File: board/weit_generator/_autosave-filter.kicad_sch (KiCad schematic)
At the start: 5 parts, among them U1 MCP6004

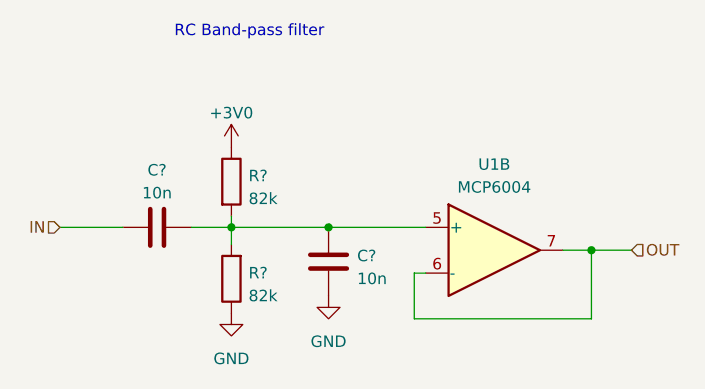
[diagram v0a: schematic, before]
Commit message: added filtering
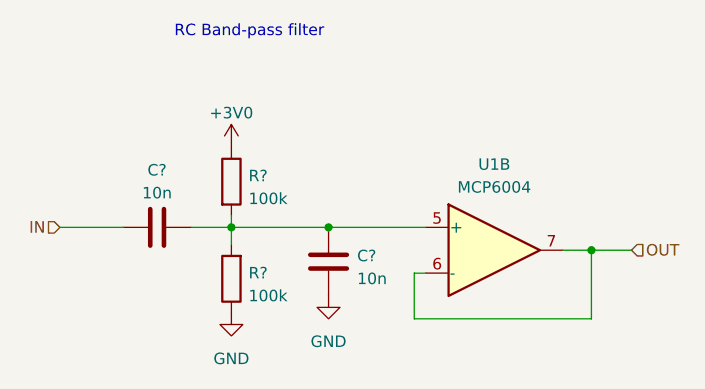
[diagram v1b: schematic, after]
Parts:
- R? (x2): value 82k -> 100k
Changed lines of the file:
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@@
       (effects (font (size 1.27 1.27)) (justify left))
     )
-    (property "Value" "82k" (at 127 93.345 0)
+    (property "Value" "100k" (at 127 93.345 0)
       (effects (font (size 1.27 1.27)) (justify left))
     )
@@
       (effects (font (size 1.27 1.27)) (justify right))
     )
-    (property "Value" "82k" (at 127 104.14 0)
+    (property "Value" "100k" (at 127 104.14 0)
       (effects (font (size 1.27 1.27)) (justify right))
     )
